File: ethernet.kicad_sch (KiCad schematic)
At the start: 45 parts

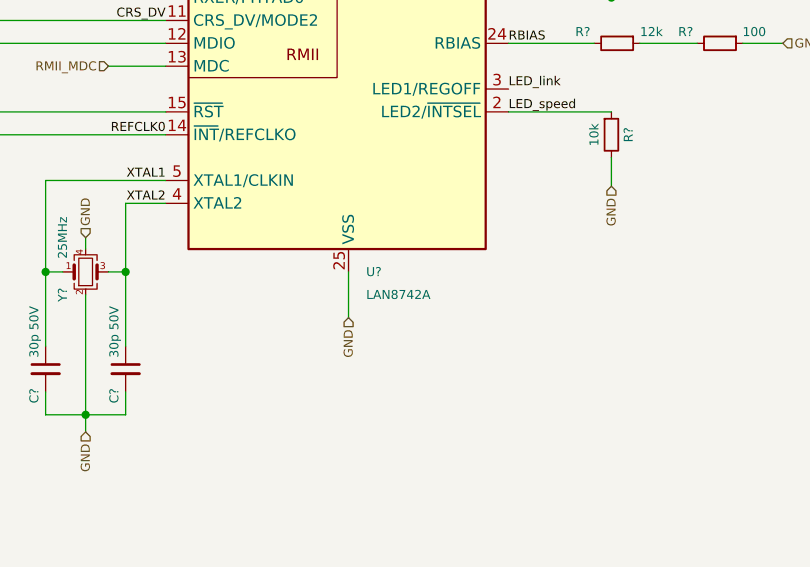
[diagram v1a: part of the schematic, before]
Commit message: #7 Change ethernet signal transformer
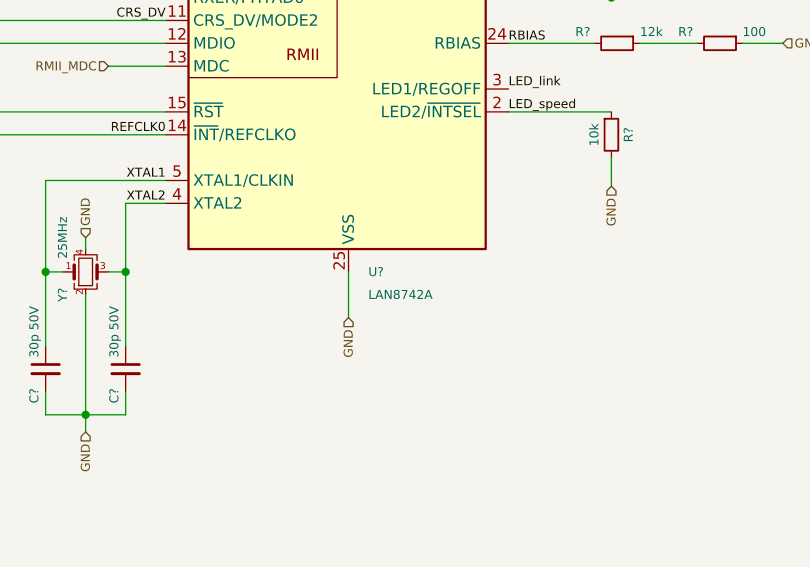
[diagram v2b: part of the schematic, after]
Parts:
- TR201: symbol #Transformer:YDS-Tech 11FB-05NL -> #Transformer:E-NETTR VP6019 HF; JLCPCB Part # C97692 -> C4154986; Manufacturer Shanghai YDS Tech -> E-NETTR; Partnumber 11FB-05NL -> VP6019 HF
- U?: footprint Package_DFN_QFN:VQFN-24-1EP_4x4mm_P0.5mm_EP2.45x2.45mm_ThermalVias -> #IC:LAN8742AI-CZ-TR; symbol Interface_Ethernet:LAN8742A -> #IC:Microchip LAN8742A
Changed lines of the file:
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@@
 	)
 	(symbol
-		(lib_id "#Transformer:YDS-Tech 11FB-05NL")
+		(lib_id "#Transformer:E-NETTR VP6019 HF")
 		(at 203.2 71.12 0)
 		(unit 1)
@@
 			)
 		)
-		(property "Datasheet" "${KIPRJMOD}/KiCad-Lib/#Transformer.doc/YDS-Tech 11FB-05NL.pdf"
+		(property "Datasheet" "${KIPRJMOD}/KiCad-Lib/#Transformer.doc/E-NETTR VP6019 HF.pdf"
 			(at 203.2 49.53 0)
 			(effects
@@
 			)
 		)
-		(property "Description" "Ethernet LAN 10/100 Base-Tx Transformer, PoE 350mA"
+		(property "Description" "Ethernet LAN 10/100 Base-Tx Transformer, PoE 850mA"
 			(at 203.2 58.42 0)
 			(effects
@@
 			)
 		)
-		(property "Manufacturer" "Shanghai YDS Tech"
+		(property "Manufacturer" "E-NETTR"
 			(at 203.2 86.36 0)
 			(effects
@@
 			)
 		)
-		(property "Partnumber" "11FB-05NL"
+		(property "Partnumber" "VP6019 HF"
 			(at 203.2 92.71 0)
 			(effects
@@
 			)
 		)
-		(property "JLCPCB Part #" "C97692"
+		(property "JLCPCB Part #" "C4154986"
 			(at 203.2 85.09 0)
 			(show_name yes)
@@
 	)
 	(symbol
-		(lib_id "Interface_Ethernet:LAN8742A")
+		(lib_id "#IC:Microchip LAN8742A")
 		(at 97.155 81.28 0)
 		(unit 1)
@@
 		(fields_autoplaced yes)
 		(property "Reference" "U?"
-			(at 99.1109 109.22 0)
+			(at 99.3491 109.22 0)
 			(effects
 				(font
@@
 		)
 		(property "Value" "LAN8742A"
-			(at 99.1109 111.76 0)
+			(at 99.3491 111.76 0)
 			(effects
 				(font
@@
 			)
 		)
-		(property "Footprint" "Package_DFN_QFN:VQFN-24-1EP_4x4mm_P0.5mm_EP2.45x2.45mm_ThermalVias"
+		(property "Footprint" "#IC:LAN8742AI-CZ-TR"
 			(at 98.425 107.95 0)
 			(effects
 				(font
-					(size 1 1)
+					(size 1.27 1.27)
 				)
 				(justify left)
@@
 			(effects
 				(font
-					(size 1 1)
-				)
-				(hide yes)
-			)
-		)
-		(property "Description" ""
+					(size 1.27 1.27)
+				)
+				(hide yes)
+			)
+		)
+		(property "Description" "LAN8720 Ethernet PHY with RMII interface, QFN-24"
 			(at 97.155 81.28 0)
 			(effects
 				(font
-					(size 1 1)
-				)
-				(hide yes)
+					(size 1.27 1.27)
+				)
+				(hide yes)
